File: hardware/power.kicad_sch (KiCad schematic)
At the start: 0 parts

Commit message: Version 1 of driver and current sense.
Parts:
- added R? (x2): 10k, symbol Device:R_Small_US
- added U? (x2): RC4558, symbol Amplifier_Operational:RC4558
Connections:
- new net: R?.1, R?.2, U?.3 (+)
- new net +3V3: R?.1, U?.8 (V+)
- new net GND: R?.2, U?.4 (V-)
- new net VAA: U?.1, U?.2 (-)
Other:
- note added: "Vaa is 1.65V for half scale reference for bidirectional current sensor."
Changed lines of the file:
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@@
 (kicad_sch (version 20211123) (generator eeschema)
   (paper "A4")
+  (junction (at 200.66 40.64) (diameter 0) (color 0 0 0 0)
+  )
+  (junction (at 228.6 38.1) (diameter 0) (color 0 0 0 0)
+  )
+  (wire (pts (xy 200.66 48.26) (xy 223.52 48.26))
+    (stroke (width 0) (type default) (color 0 0 0 0))
+  )
+  (wire (pts (xy 228.6 27.94) (xy 228.6 30.48))
+    (stroke (width 0) (type default) (color 0 0 0 0))
+  )
+  (wire (pts (xy 228.6 35.56) (xy 228.6 38.1))
+    (stroke (width 0) (type default) (color 0 0 0 0))
+  )
+  (wire (pts (xy 254 45.72) (xy 254 48.26))
+    (stroke (width 0) (type default) (color 0 0 0 0))
+  )
+  (wire (pts (xy 223.52 43.18) (xy 220.98 43.18))
+    (stroke (width 0) (type default) (color 0 0 0 0))
+  )
+  (wire (pts (xy 228.6 45.72) (xy 228.6 48.26))
+    (stroke (width 0) (type default) (color 0 0 0 0))
+  )
+  (wire (pts (xy 223.52 48.26) (xy 223.52 43.18))
+    (stroke (width 0) (type default) (color 0 0 0 0))
+  )
+  (wire (pts (xy 254 27.94) (xy 254 30.48))
+    (stroke (width 0) (type default) (color 0 0 0 0))
+  )
+  (wire (pts (xy 200.66 40.64) (xy 200.66 48.26))
+    (stroke (width 0) (type default) (color 0 0 0 0))
+  )
+  (wire (pts (xy 200.66 40.64) (xy 205.74 40.64))
+    (stroke (width 0) (type default) (color 0 0 0 0))
+  )
+  (wire (pts (xy 220.98 38.1) (xy 228.6 38.1))
+    (stroke (width 0) (type default) (color 0 0 0 0))
+  )
+  (wire (pts (xy 200.66 38.1) (xy 200.66 40.64))
+    (stroke (width 0) (type default) (color 0 0 0 0))
+  )
+  (wire (pts (xy 228.6 38.1) (xy 228.6 40.64))
+    (stroke (width 0) (type default) (color 0 0 0 0))
+  )
+  (text "Vaa is 1.65V for half scale reference for\nbidirectional current sensor."
+    (at 203.2 20.32 0)
+    (effects (font (size 1.27 1.27)) (justify left bottom))
+  )
+  (symbol (lib_id "power:GND") (at 228.6 48.26 0) (unit 1)
+    (in_bom yes) (on_board yes) (fields_autoplaced)
+    (property "Reference" "#PWR?" (id 0) (at 228.6 54.61 0)
+      (effects (font (size 1.27 1.27)) hide)
+    )
+    (property "Value" "GND" (id 1) (at 228.6 53.34 0))
+    (property "Footprint" "" (id 2) (at 228.6 48.26 0)
+      (effects (font (size 1.27 1.27)) hide)
+    )
+    (property "Datasheet" "" (id 3) (at 228.6 48.26 0)
+      (effects (font (size 1.27 1.27)) hide)
+    )
+    (pin "1")
+  )
+  (symbol (lib_id "Amplifier_Operational:RC4558") (at 256.54 38.1 0) (unit 3)
+    (in_bom yes) (on_board yes) (fields_autoplaced)
+    (property "Reference" "U?" (id 0) (at 255.27 36.8299 0)
+      (effects (font (size 1.27 1.27)) (justify left))
+    )
+    (property "Value" "RC4558" (id 1) (at 255.27 39.3699 0)
+      (effects (font (size 1.27 1.27)) (justify left))
+    )
+    (property "Footprint" "" (id 2) (at 256.54 38.1 0)
+      (effects (font (size 1.27 1.27)) hide)
+    )
+    (property "Datasheet" "http://www.ti.com/lit/ds/symlink/rc4558.pdf" (id 3) (at 256.54 38.1 0)
+      (effects (font (size 1.27 1.27)) hide)
+    )
+    (pin "1")
+    (pin "2")
+    (pin "3")
+    (pin "5")
+    (pin "6")
+    (pin "7")
+    (pin "4")
+    (pin "8")
+  )
+  (symbol (lib_id "Device:R_Small_US") (at 228.6 33.02 0) (unit 1)
+    (in_bom yes) (on_board yes) (fields_autoplaced)
+    (property "Reference" "R?" (id 0) (at 231.14 31.7499 0)
+      (effects (font (size 1.27 1.27)) (justify left))
+    )
+    (property "Value" "10k" (id 1) (at 231.14 34.2899 0)
+      (effects (font (size 1.27 1.27)) (justify left))
+    )
+    (property "Footprint" "" (id 2) (at 228.6 33.02 0)
+      (effects (font (size 1.27 1.27)) hide)
+    )
+    (property "Datasheet" "~" (id 3) (at 228.6 33.02 0)
+      (effects (font (size 1.27 1.27)) hide)
+    )
+    (pin "1")
+    (pin "2")
+  )
+  (symbol (lib_id "Amplifier_Operational:RC4558") (at 213.36 40.64 0) (mirror y) (unit 1)
+    (in_bom yes) (on_board yes) (fields_autoplaced)
+    (property "Reference" "U?" (id 0) (at 213.36 30.48 0))
+    (property "Value" "RC4558" (id 1) (at 213.36 33.02 0))
+    (property "Footprint" "" (id 2) (at 213.36 40.64 0)
+      (effects (font (size 1.27 1.27)) hide)
+    )
+    (property "Datasheet" "http://www.ti.com/lit/ds/symlink/rc4558.pdf" (id 3) (at 213.36 40.64 0)
+      (effects (font (size 1.27 1.27)) hide)
+    )
+    (pin "1")
+    (pin "2")
+    (pin "3")
+    (pin "5")
+    (pin "6")
+    (pin "7")
+    (pin "4")
+    (pin "8")
+  )
+  (symbol (lib_id "power:VAA") (at 200.66 38.1 0) (unit 1)
+    (in_bom yes) (on_board yes) (fields_autoplaced)
+    (property "Reference" "#PWR?" (id 0) (at 200.66 41.91 0)
+      (effects (font (size 1.27 1.27)) hide)
+    )
+    (property "Value" "VAA" (id 1) (at 200.66 33.02 0))
+    (property "Footprint" "" (id 2) (at 200.66 38.1 0)
+      (effects (font (size 1.27 1.27)) hide)
+    )
+    (property "Datasheet" "" (id 3) (at 200.66 38.1 0)
+      (effects (font (size 1.27 1.27)) hide)
+    )
+    (pin "1")
+  )
+  (symbol (lib_id "power:+3.3V") (at 228.6 27.94 0) (unit 1)
+    (in_bom yes) (on_board yes) (fields_autoplaced)
+    (property "Reference" "#PWR?" (id 0) (at 228.6 31.75 0)
+      (effects (font (size 1.27 1.27)) hide)
+    )
+    (property "Value" "+3.3V" (id 1) (at 228.6 22.86 0))
+    (property "Footprint" "" (id 2) (at 228.6 27.94 0)
+      (effects (font (size 1.27 1.27)) hide)
+    )
+    (property "Datasheet" "" (id 3) (at 228.6 27.94 0)
+      (effects (font (size 1.27 1.27)) hide)
+    )
+    (pin "1")
+  )
+  (symbol (lib_id "power:GND") (at 254 48.26 0) (unit 1)
+    (in_bom yes) (on_board yes) (fields_autoplaced)
+    (property "Reference" "#PWR?" (id 0) (at 254 54.61 0)
+      (effects (font (size 1.27 1.27)) hide)
+    )
+    (property "Value" "GND" (id 1) (at 254 53.34 0))
+    (property "Footprint" "" (id 2) (at 254 48.26 0)
+      (effects (font (size 1.27 1.27)) hide)
+    )
+    (property "Datasheet" "" (id 3) (at 254 48.26 0)
+      (effects (font (size 1.27 1.27)) hide)
+    )
+    (pin "1")
+  )
+  (symbol (lib_id "Device:R_Small_US") (at 228.6 43.18 0) (unit 1)
+    (in_bom yes) (on_board yes) (fields_autoplaced)
+    (property "Reference" "R?" (id 0) (at 231.14 41.9099 0)
+      (effects (font (size 1.27 1.27)) (justify left))
+    )
+    (property "Value" "10k" (id 1) (at 231.14 44.4499 0)
+      (effects (font (size 1.27 1.27)) (justify left))
+    )
+    (property "Footprint" "" (id 2) (at 228.6 43.18 0)
+      (effects (font (size 1.27 1.27)) hide)
+    )
+    (property "Datasheet" "~" (id 3) (at 228.6 43.18 0)
+      (effects (font (size 1.27 1.27)) hide)
+    )
+    (pin "1")
+    (pin "2")
+  )
+  (symbol (lib_id "power:+3.3V") (at 254 27.94 0) (unit 1)
+    (in_bom yes) (on_board yes) (fields_autoplaced)
+    (property "Reference" "#PWR?" (id 0) (at 254 31.75 0)
+      (effects (font (size 1.27 1.27)) hide)
+    )
+    (property "Value" "+3.3V" (id 1) (at 254 22.86 0))
+    (property "Footprint" "" (id 2) (at 254 27.94 0)
+      (effects (font (size 1.27 1.27)) hide)
+    )
+    (property "Datasheet" "" (id 3) (at 254 27.94 0)
+      (effects (font (size 1.27 1.27)) hide)
+    )
+    (pin "1")
+  )
 )

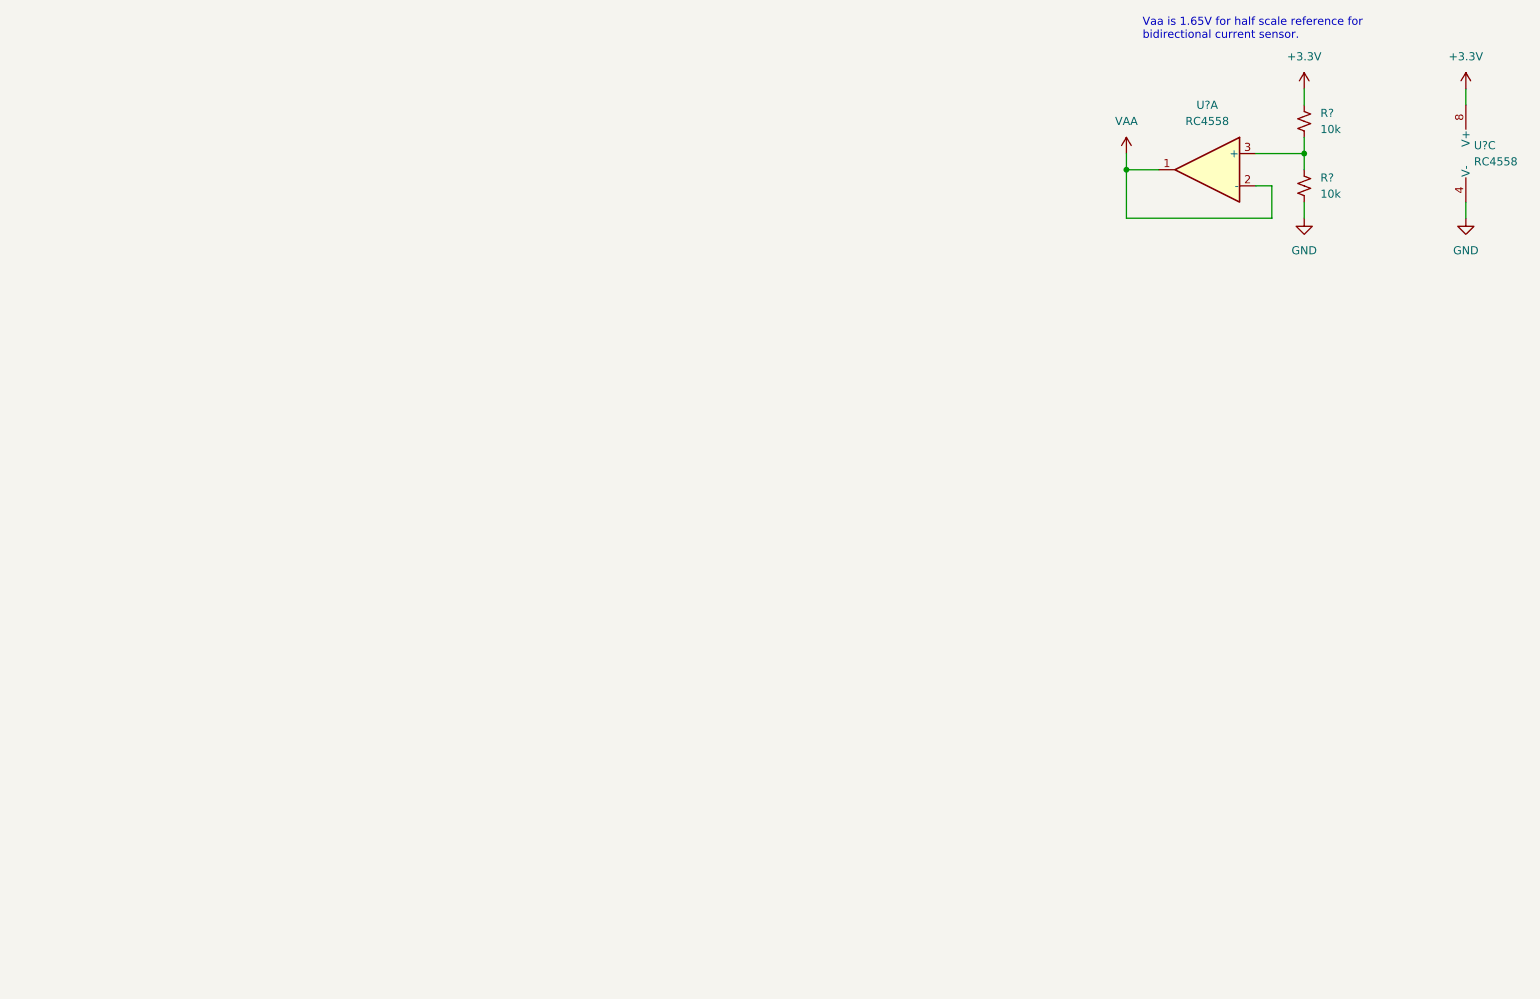
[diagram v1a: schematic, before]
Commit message: added buck converter rev1
still need to pick inductors, size bulk capacitance, verify calcs
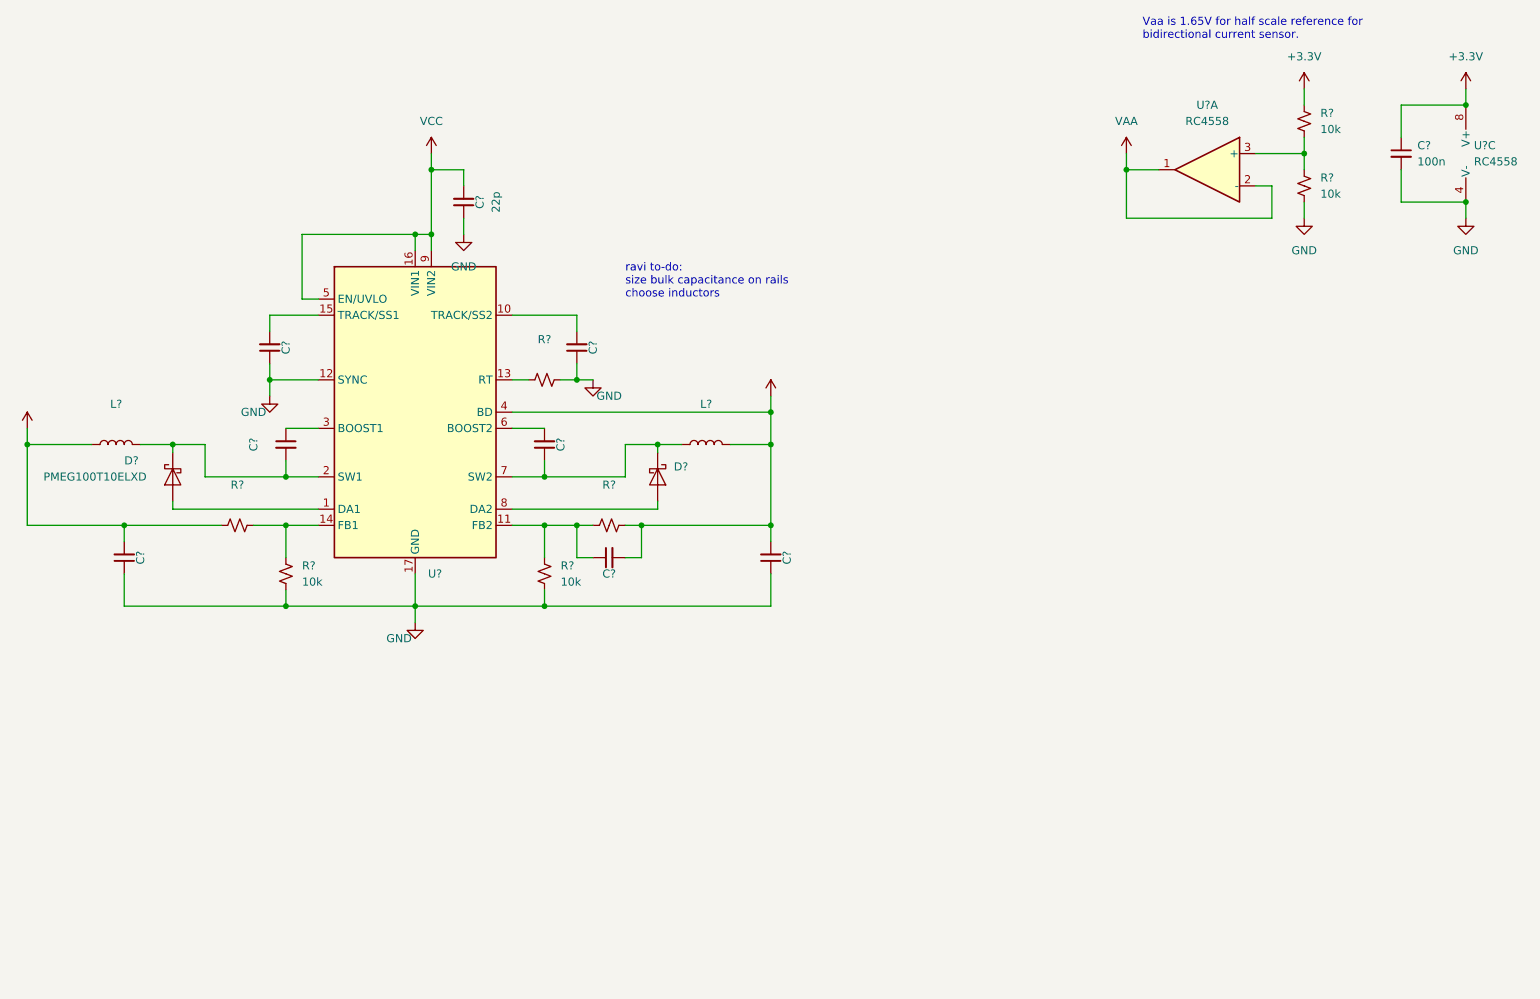
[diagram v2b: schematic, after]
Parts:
- added C? (x7): (no value), symbol Device:C_Small
- added C?: 22p, symbol Device:C_Small
- added C?: 100n, symbol Device:C_Small
- added D?: (no value), symbol Diode:PMEG6010CEJ
- added D?: PMEG100T10ELXD, Diode_SMD:D_SOD-323F, symbol Diode:PMEG6010CEJ
- added L? (x2): (no value), symbol Device:L
- added R? (x3): (no value), symbol Device:R_Small_US
- added R? (x2): 10k, symbol Device:R_Small_US
- added U?: (no value), symbol Regulator_Switching:LT3988
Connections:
- net +3V3: now also C?.1, C?.2, C?.2, L?.2, R?.1, U?.4 (BD)
- net GND: now also C?.1, C?.1, C?.1, C?.1, C?.1, C?.2, R?.1, R?.1, R?.2, U?.12 (SYNC), U?.17 (GND)
- new net: C?.1, R?.2, R?.2, U?.11 (FB2)
- new net: C?.1, D?.1 (K), L?.1, U?.7 (SW2)
- new net: D?.2 (A), U?.8 (DA2)
- new net: C?.2, U?.10 (TRACK/SS2)
- new net: R?.1, R?.2, U?.14 (FB1)
- new net: C?.2, U?.6 (BOOST2)
- new net: C?.1, U?.3 (BOOST1)
- new net: C?.2, D?.1 (K), L?.2, U?.2 (SW1)
- new net: D?.2 (A), U?.1 (DA1)
- new net: R?.1, U?.13 (RT)
- new net: C?.2, U?.15 (TRACK/SS1)
- new net VCC: C?.2, U?.16 (VIN1), U?.5 (EN/UVLO), U?.9 (VIN2)
- new net VDD: C?.2, L?.1, R?.2
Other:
- note added: "ravi to-do: size bulk capacitance on rails choose inductors"

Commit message: Started Buck Layout
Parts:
- removed L?: (no value), symbol Device:L
- added C10, C11, C13, C15, C7: 4.7u, symbol Device:C_Small
- added C6: (no value), symbol Device:C_Small
- added L1: (no value), symbol Device:L
- C14, C9: renamed from C?; value (none) -> 220n
- C16, C8: renamed from C?; value (none) -> 1n
- C17: renamed from C?; value (none) -> 22p
- C5: renamed from C?; value (none) -> ?
- D1: renamed from D?; value PMEG100T10ELXD -> (none); footprint Diode_SMD:D_SOD-323F -> (none); Mouser (none) -> https://www.mouser.com/ProductDetail/Nexperia/PMEG100T10ELX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
- D2: renamed from D?; Mouser (none) -> https://www.mouser.com/ProductDetail/Nexperia/PMEG100T10ELX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
- L2: renamed from L?; Mouser (none) -> https://www.mouser.com/ProductDetail/Coilcraft/XFL3012-103M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
- R1: renamed from R?; value (none) -> 150k
- R3, R5: renamed from R?; value (none) -> 34k
- U2: renamed from U?; value (none) -> LT3988; footprint (none) -> Package_SO:MSOP-16-1EP_3x4mm_P0.5mm_EP1.65x2.85mm
- gave numbers to parts that had none: 8
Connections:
- net GND: now also C10.2, C11.2, C13.2, C15.2, C6.2, C7.2
- net VCC: now also C10.1, C11.1, C13.1, C15.1, C6.1, C7.1
- net VDD: now also L1.1
- net at C9.2, D1.1 (K), U2.2 (SW1): now also L1.2
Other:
- note added: "all resistors 1%"
- note added: "already selected"
- note added: "bulk capacitance to be placed close to fets"
- note added: "capacitors will be exposed to 60V, X7R"
- note added: "res 1% or better cap for 3.3V"
- note removed: "ravi to-do: size bulk capacitance on rails choose inductors"
